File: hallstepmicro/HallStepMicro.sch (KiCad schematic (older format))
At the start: 44 parts, among them IC1 ATTINY84A-SS, K1 CONN_3, K2 CONN_3, K3 CONN_3, K4 CONN_3

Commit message: More rework.
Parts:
- removed CD1, CD2, CD3, CD4: 0.1u, ~, symbol C
- removed CH1, CH2, CH3, CH4: 10p, ~, symbol C
- removed HALL6OUT1: CONN_6, symbol CONN_6
- removed JDIR1, JENB1, JGND1, JMAX1, JMIN1, JPDC1, JPDC2, JPDC3, JPDC4, JPHALL1, JPHALL2, JPHALL3, JPHALL4, JPWR1, JSTEP1: JUMPER, ~, symbol JUMPER
- removed K1, K2, K3, K4: CONN_3, symbol CONN_3
- removed UHall1, UHall2, UHall3, UHall4: A3213, ~, symbol A3213
- added JDC1: CONN_4X2, symbol CONN_4X2
- added JHALLS1: CONN_6X2, symbol CONN_6X2
- added JSTEP1: CONN_5X2, symbol CONN_5X2
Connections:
- net labels removed: hall1_out, hall2_out, hall3_out, hall4_out
- wire segments 144 -> 84
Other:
- note removed: "Thru-holes for\nTO-92 case style."
- moved on the sheet: DCM1, HALL6IN1, IC1, ISP6PIN1, RBRK1, RENB1, RESET1, RMODE1, RPHASE1, RRESET1, SENSE1, STEPIN1

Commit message: Working on layout.
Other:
- moved on the sheet: RENB1, RMODE1
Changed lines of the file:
@@
-EESchema Schematic File Version 2  date Sunday, 29 September, 2013 10:37:23 pm
+EESchema Schematic File Version 2  date Monday, 30 September, 2013 11:09:14 am
 LIBS:power
 LIBS:device
@@
 Text Label 8800 2100 0    60   ~ 0
 DC_BRAKE
-Text Label 8800 2200 0    60   ~ 0
+Text Label 8800 2400 0    60   ~ 0
 DC_ENABLE
 Text Label 8800 2300 0    60   ~ 0
 DC_PHASE
-Text Label 8800 2400 0    60   ~ 0
+Text Label 8800 2200 0    60   ~ 0
 DC_MODE
-Text Notes 8450 2600 0    60   ~ 0
+Text Notes 8000 2600 0    60   ~ 0
 Control Signals for\nAllegro A4973
 $Comp
@@
 Text Label 8800 5300 0    60   ~ 0
 ENB
-Text Label 7450 2200 0    60   ~ 0
+Text Label 7450 2400 0    60   ~ 0
 PWM
 Text Label 8800 5200 0    60   ~ 0
@@
 Text Label 7450 2100 0    60   ~ 0
 BRAKE
-Text Label 7450 2400 0    60   ~ 0
+Text Label 7450 2200 0    60   ~ 0
 MODE
 Text Label 8800 5400 0    60   ~ 0
@@
 L VDD #PWR08
 U 1 1 524726B7
-P 6700 2200
-F 0 "#PWR08" H 6700 2300 30  0001 C CNN
-F 1 "VDD" H 6700 2310 30  0000 C CNN
-F 2 "" H 6700 2200 60  0000 C CNN
-F 3 "" H 6700 2200 60  0000 C CNN
-	1    6700 2200
+P 6700 2400
+F 0 "#PWR08" H 6700 2500 30  0001 C CNN
+F 1 "VDD" H 6700 2510 30  0000 C CNN
+F 2 "" H 6700 2400 60  0000 C CNN
+F 3 "" H 6700 2400 60  0000 C CNN
+	1    6700 2400
 	1    0    0    -1
 $EndComp
@@
 L R RENB1
 U 1 1 524726A8
-P 7150 2200
-F 0 "RENB1" V 7230 2200 40  0000 C CNN
-F 1 "5K" V 7157 2201 40  0000 C CNN
-F 2 "~" V 7080 2200 30  0000 C CNN
-F 3 "~" H 7150 2200 30  0000 C CNN
-	1    7150 2200
+P 7150 2400
+F 0 "RENB1" V 7230 2400 40  0000 C CNN
+F 1 "5K" V 7157 2401 40  0000 C CNN
+F 2 "~" V 7080 2400 30  0000 C CNN
+F 3 "~" H 7150 2400 30  0000 C CNN
+	1    7150 2400
 	0    -1   -1   0
 $EndComp
@@
 L VDD #PWR010
 U 1 1 5247292E
-P 6700 2400
-F 0 "#PWR010" H 6700 2500 30  0001 C CNN
-F 1 "VDD" H 6700 2510 30  0000 C CNN
-F 2 "" H 6700 2400 60  0000 C CNN
-F 3 "" H 6700 2400 60  0000 C CNN
-	1    6700 2400
+P 6700 2200
+F 0 "#PWR010" H 6700 2300 30  0001 C CNN
+F 1 "VDD" H 6700 2310 30  0000 C CNN
+F 2 "" H 6700 2200 60  0000 C CNN
+F 3 "" H 6700 2200 60  0000 C CNN
+	1    6700 2200
 	1    0    0    -1
 $EndComp
@@
 L R RMODE1
 U 1 1 52472934
-P 7150 2400
-F 0 "RMODE1" V 7230 2400 40  0000 C CNN
-F 1 "5K" V 7157 2401 40  0000 C CNN
-F 2 "~" V 7080 2400 30  0000 C CNN
-F 3 "~" H 7150 2400 30  0000 C CNN
-	1    7150 2400
+P 7150 2200
+F 0 "RMODE1" V 7230 2200 40  0000 C CNN
+F 1 "5K" V 7157 2201 40  0000 C CNN
+F 2 "~" V 7080 2200 30  0000 C CNN
+F 3 "~" H 7150 2200 30  0000 C CNN
+	1    7150 2200
 	0    -1   -1   0
 $EndComp
@@
 	8700 2300 9300 2300
 Wire Wire Line
-	8700 2200 9300 2200
+	8700 2400 9300 2400
 Wire Wire Line
 	8700 2100 9300 2100
 Wire Wire Line
-	9300 2400 8700 2400
+	9300 2200 8700 2200
 Wire Wire Line
 	7950 3000 7750 3000
@@
 	7400 2300 7900 2300
 Wire Wire Line
-	7400 2400 7900 2400
+	7400 2200 7900 2200
 Wire Wire Line
 	7400 2100 7900 2100
 Wire Wire Line
-	7900 2200 7400 2200
+	7900 2400 7400 2400
 Wire Wire Line
 	4100 5300 4600 5300
@@
 	6700 2100 6900 2100
 Wire Wire Line
-	6900 2200 6700 2200
+	6900 2400 6700 2400
 Wire Wire Line
 	6900 2300 6700 2300
 Wire Wire Line
-	6700 2400 6900 2400
+	6700 2200 6900 2200
 $Comp
 L CONN_2 RESET1

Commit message: Simplify. Simplify. Simplify.
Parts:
- removed JDC1: CONN_4X2, symbol CONN_4X2
- removed JHALLS1: CONN_6X2, symbol CONN_6X2
- removed JSTEP1: CONN_5X2, symbol CONN_5X2
- added HALL6OUT1: CONN_6, symbol CONN_6
- added RDIR1: 0.0, ~, symbol R
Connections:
- net labels added: STP_ENB, hall1_out, hall2_out, hall3_out, hall4_out
- net labels removed: BRAKE, ENB, MISO, MODE, MOSI, PHASE_DIR, PWM, SCK, STP_ENABLE
- wire segments 84 -> 62
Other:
- note added: "MISO"
- note added: "MOSI"
- note added: "SCK"
- moved on the sheet: DCM1, RBRK1, RENB1, RMODE1, RPHASE1, STEPIN1

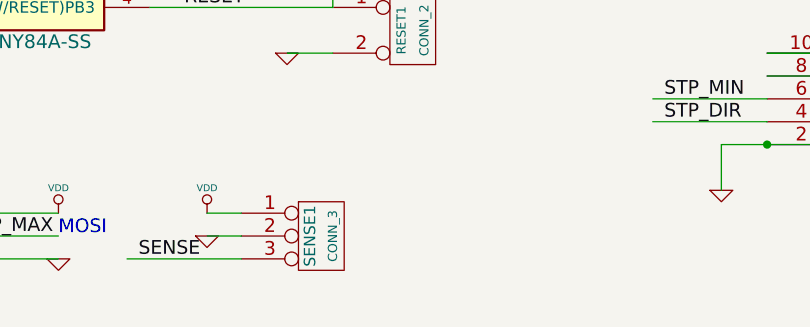
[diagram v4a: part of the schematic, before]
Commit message: Added comment about using Freescale MPX5500 pressure sensor.
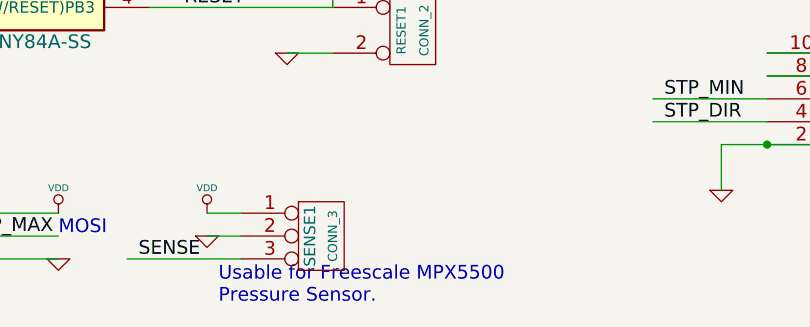
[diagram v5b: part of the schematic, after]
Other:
- note added: "Usable for Freescale MPX5500\nPressure Sensor."
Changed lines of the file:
@@
-EESchema Schematic File Version 2  date Tuesday, 01 October, 2013 11:17:25 am
+EESchema Schematic File Version 2  date Tuesday, 01 October, 2013 02:42:25 pm
 LIBS:power
 LIBS:device
@@
 Wire Wire Line
 	6900 5200 6400 5200
+Text Notes 4400 6700 0    60   ~ 0
+Usable for Freescale MPX5500\nPressure Sensor.
 $EndSCHEMATC

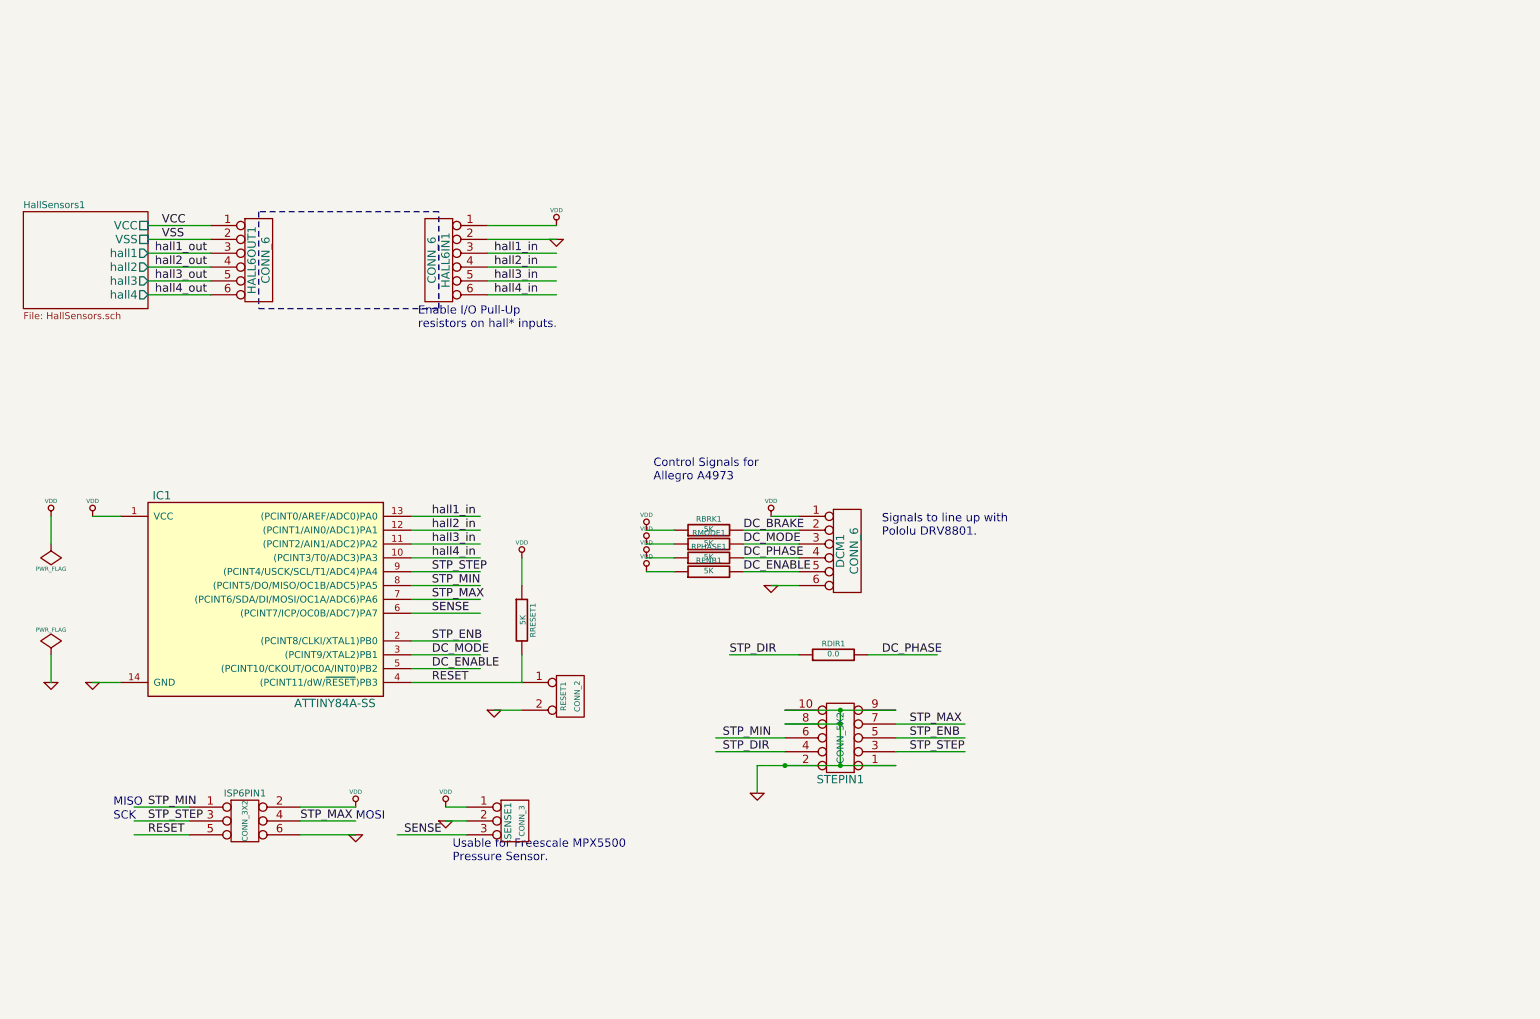
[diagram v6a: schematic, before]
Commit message: Adding some documentation & related markup.
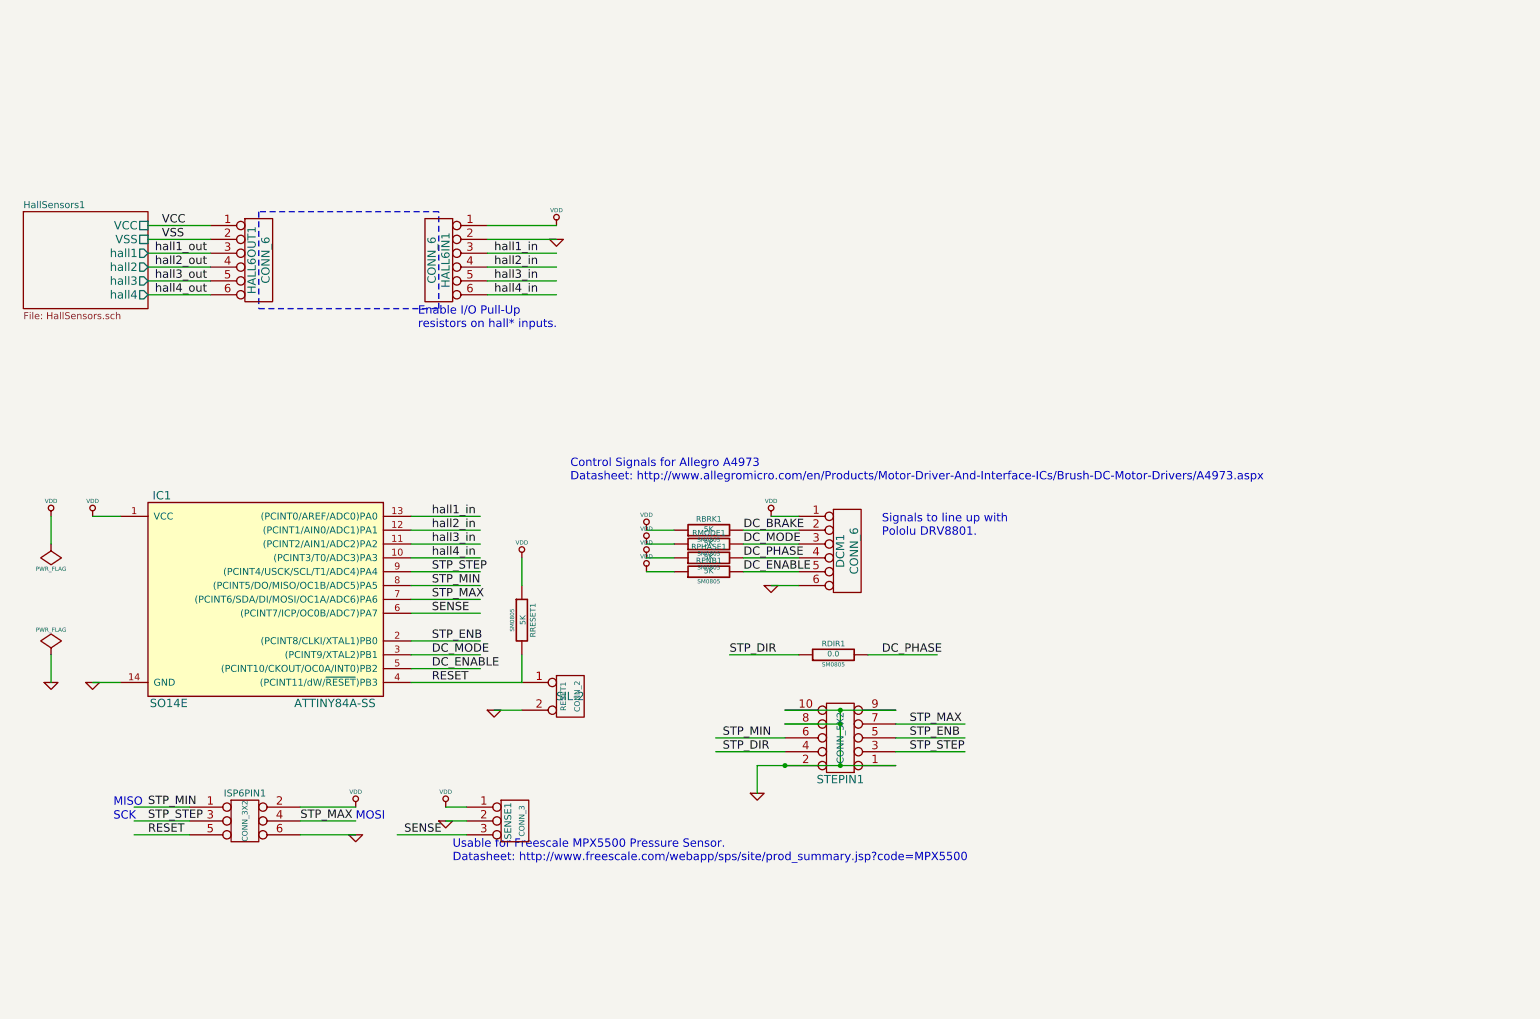
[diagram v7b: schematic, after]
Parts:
- DCM1, HALL6IN1, HALL6OUT1: footprint (none) -> SIL6-offset-0p005
- IC1: footprint SO14 -> SO14E
- ISP6PIN1: footprint (none) -> pin_array_3x2-offset-0p005
- RBRK1, RDIR1, RENB1, RMODE1, RPHASE1, RRESET1: footprint ~ -> SM0805
- RESET1: footprint (none) -> SIL-2
- SENSE1: footprint (none) -> SIL3-offset-0p005
- STEPIN1: footprint (none) -> PIN_ARRAY_5x2-offset-0p005
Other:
- note added: "Control Signals for Allegro A4973\nDatasheet: http://www.allegromicro.com/en/Products/Motor-Driver-And-Interface-ICs/Brush-DC-Motor-Drivers/A4973.aspx"
- note added: "Usable for Freescale MPX5500 Pressure Sensor.\nDatasheet: http://www.freescale.com/webapp/sps/site/prod_summary.jsp?code=MPX5500"
- note removed: "Control Signals for\nAllegro A4973"
- note removed: "Usable for Freescale MPX5500\nPressure Sensor."
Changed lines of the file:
@@
-EESchema Schematic File Version 2  date Wednesday, 02 October, 2013 09:18:38 pm
+EESchema Schematic File Version 2  date Friday, 04 October, 2013 11:24:01 am
 LIBS:power
 LIBS:device
@@
 encoding utf-8
 Sheet 1 2
-Title ""
-Date "3 oct 2013"
-Rev ""
-Comp ""
+Title "Hall Sensors With ATtiny84A Support"
+Date "4 oct 2013"
+Rev "20131004"
+Comp "ClothBot Designs"
 Comment1 ""
 Comment2 ""
@@
 F 0 "IC1" H 2300 5550 60  0000 C CNN
 F 1 "ATTINY84A-SS" H 3550 4050 60  0000 C CNN
-F 2 "SO14" H 2350 4050 60  0001 C CNN
-F 3 "" H 3050 4800 60  0000 C CNN
+F 2 "SO14E" H 2350 4050 60  0000 C CNN
+F 3 "http://www.atmel.com/devices/ATTINY84A.aspx" H 3050 4800 60  0001 C CNN
 	1    3050 4800
 	1    0    0    -1
@@
 F 0 "ISP6PIN1" H 2900 6700 50  0000 C CNN
 F 1 "CONN_3X2" V 2900 6500 40  0000 C CNN
-F 2 "" H 2900 6450 60  0000 C CNN
+F 2 "pin_array_3x2-offset-0p005" H 2900 6450 60  0001 C CNN
 F 3 "" H 2900 6450 60  0000 C CNN
 	1    2900 6450
@@
 Text Label 4250 5400 0    60   ~ 0
 RESET
-Text Notes 5850 3950 0    60   ~ 0
-Control Signals for\nAllegro A4973
+Text Notes 5250 3950 0    60   ~ 0
+Control Signals for Allegro A4973\nDatasheet: http://www.allegromicro.com/en/Products/Motor-Driver-And-Interface-ICs/Brush-DC-Motor-Drivers/A4973.aspx
 $Comp
 L CONN_6 DCM1
@@
 F 0 "DCM1" V 7200 4450 60  0000 C CNN
 F 1 "CONN_6" V 7300 4450 60  0000 C CNN
-F 2 "" H 7250 4450 60  0000 C CNN
+F 2 "SIL6-offset-0p005" V 7250 4450 60  0001 C CNN
 F 3 "" H 7250 4450 60  0000 C CNN
 	1    7250 4450
@@
 F 0 "STEPIN1" H 7200 6100 60  0000 C CNN
 F 1 "CONN_5X2" V 7200 5800 50  0000 C CNN
-F 2 "" H 7200 5800 60  0000 C CNN
+F 2 "PIN_ARRAY_5x2-offset-0p005" H 7200 5800 60  0001 C CNN
 F 3 "" H 7200 5800 60  0000 C CNN
 	1    7200 5800
@@
 F 0 "RENB1" V 6330 4600 40  0000 C CNN
 F 1 "5K" V 6257 4601 40  0000 C CNN
-F 2 "~" V 6180 4600 30  0000 C CNN
+F 2 "SM0805" V 6180 4600 30  0000 C CNN
 F 3 "~" H 6250 4600 30  0000 C CNN
 	1    6250 4600
@@
 F 0 "RBRK1" V 6330 4300 40  0000 C CNN
 F 1 "5K" V 6257 4301 40  0000 C CNN
-F 2 "~" V 6180 4300 30  0000 C CNN
+F 2 "SM0805" V 6180 4300 30  0000 C CNN
 F 3 "~" H 6250 4300 30  0000 C CNN
 	1    6250 4300
@@
 F 0 "RMODE1" V 6330 4400 40  0000 C CNN
 F 1 "5K" V 6257 4401 40  0000 C CNN
-F 2 "~" V 6180 4400 30  0000 C CNN
+F 2 "SM0805" V 6180 4400 30  0000 C CNN
 F 3 "~" H 6250 4400 30  0000 C CNN
 	1    6250 4400
@@
 F 0 "RPHASE1" V 6330 4500 40  0000 C CNN
 F 1 "5K" V 6257 4501 40  0000 C CNN
-F 2 "~" V 6180 4500 30  0000 C CNN
+F 2 "SM0805" V 6180 4500 30  0000 C CNN
 F 3 "~" H 6250 4500 30  0000 C CNN
 	1    6250 4500
@@
 F 0 "RRESET1" V 4980 4950 40  0000 C CNN
 F 1 "5K" V 4907 4951 40  0000 C CNN
-F 2 "~" V 4830 4950 30  0000 C CNN
+F 2 "SM0805" V 4830 4950 30  0000 C CNN
 F 3 "~" H 4900 4950 30  0000 C CNN
 	1    4900 4950
@@
 F 0 "SENSE1" V 4800 6400 50  0000 C CNN
 F 1 "CONN_3" V 4900 6400 40  0000 C CNN
-F 2 "" H 4850 6400 60  0000 C CNN
-F 3 "" H 4850 6400 60  0000 C CNN
+F 2 "SIL3-offset-0p005" H 4850 6400 60  0001 C CNN
+F 3 "http://www.freescale.com/webapp/sps/site/prod_summary.jsp?code=MPX5500" H 4850 6400 60  0001 C CNN
 	1    4850 6400
 	1    0    0    -1
@@
 F 0 "HALL6IN1" V 4250 2350 60  0000 C CNN
 F 1 "CONN_6" V 4350 2350 60  0000 C CNN
-F 2 "" H 4300 2350 60  0000 C CNN
+F 2 "SIL6-offset-0p005" V 4300 2350 60  0001 C CNN
 F 3 "" H 4300 2350 60  0000 C CNN
 	1    4300 2350
@@
 F 0 "RESET1" V 5200 5500 40  0000 C CNN
 F 1 "CONN_2" V 5300 5500 40  0000 C CNN
-F 2 "" H 5250 5500 60  0000 C CNN
+F 2 "SIL-2" H 5250 5500 60  0000 C CNN
 F 3 "" H 5250 5500 60  0000 C CNN
 	1    5250 5500
@@
 F 0 "HALL6OUT1" V 2950 2350 60  0000 C CNN
 F 1 "CONN_6" V 3050 2350 60  0000 C CNN
-F 2 "" H 3000 2350 60  0000 C CNN
+F 2 "SIL6-offset-0p005" V 3000 2350 60  0001 C CNN
 F 3 "" H 3000 2350 60  0000 C CNN
 	1    3000 2350
@@
 F 0 "RDIR1" V 7230 5200 40  0000 C CNN
 F 1 "0.0" V 7157 5201 40  0000 C CNN
-F 2 "~" V 7080 5200 30  0000 C CNN
+F 2 "SM0805" V 7080 5200 30  0000 C CNN
 F 3 "~" H 7150 5200 30  0000 C CNN
 	1    7150 5200
@@
 	6900 5200 6400 5200
 Text Notes 4400 6700 0    60   ~ 0
-Usable for Freescale MPX5500\nPressure Sensor.
+Usable for Freescale MPX5500 Pressure Sensor.\nDatasheet: http://www.freescale.com/webapp/sps/site/prod_summary.jsp?code=MPX5500
 $EndSCHEMATC
